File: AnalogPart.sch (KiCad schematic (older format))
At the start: 9 parts, among them U15 LT6018

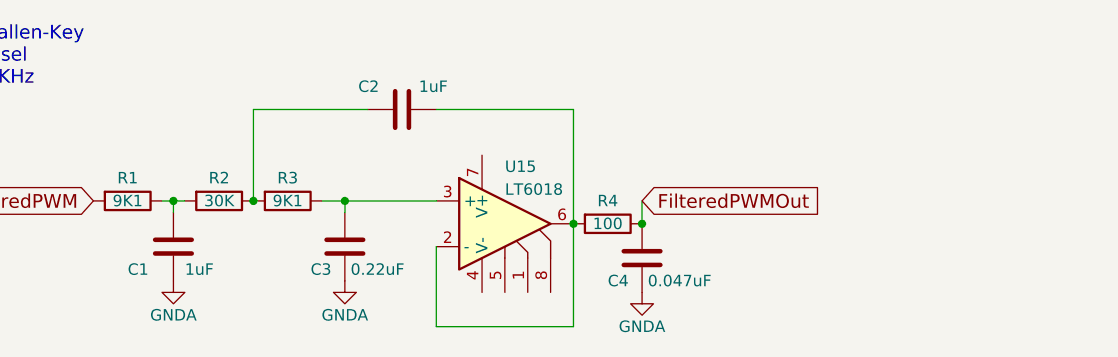
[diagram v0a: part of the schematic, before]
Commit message: Version 1. Directly drive PWM filter using 74hc74 flip flop
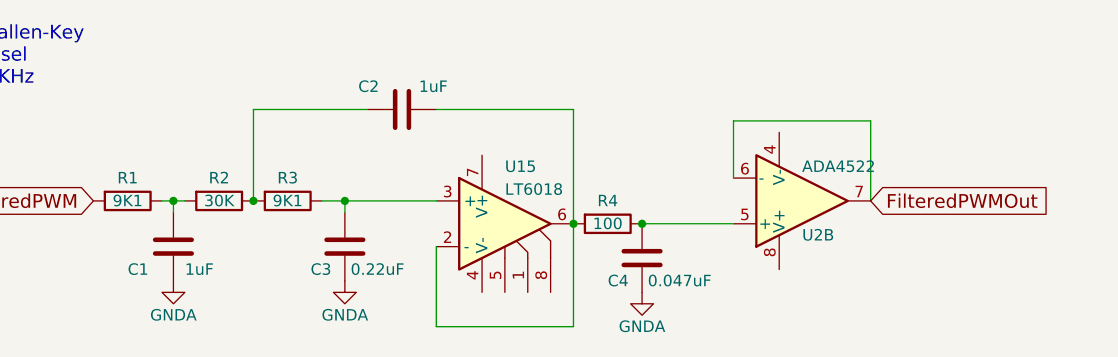
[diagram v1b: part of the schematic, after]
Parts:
- added U2: ADA4522, symbol ADA4075
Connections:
- net FilteredPWMOut: now also U2.6 (-), U2.7; no longer C4.1, R4.1
- new net: C4.1, R4.1, U2.5 (+)
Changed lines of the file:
@@
 $Descr A4 11693 8268
 encoding utf-8
-Sheet 2 3
+Sheet 2 2
 Title ""
 Date ""
@@
 $EndComp
 $Comp
-L GNDA #PWR13
+L GNDA #PWR21
 U 1 1 5A91C21B
 P 2350 2700
-F 0 "#PWR13" H 2350 2450 50  0001 C CNN
+F 0 "#PWR21" H 2350 2450 50  0001 C CNN
 F 1 "GNDA" H 2350 2550 50  0000 C CNN
 F 2 "" H 2350 2700 50  0001 C CNN
@@
 $EndComp
 $Comp
-L GNDA #PWR14
+L GNDA #PWR22
 U 1 1 5A91C23F
 P 3100 2700
-F 0 "#PWR14" H 3100 2450 50  0001 C CNN
+F 0 "#PWR22" H 3100 2450 50  0001 C CNN
 F 1 "GNDA" H 3100 2550 50  0000 C CNN
 F 2 "" H 3100 2700 50  0001 C CNN
@@
 $EndComp
 Wire Wire Line
-	2300 2350 2400 2350
+	2300 2350 2350 2350
+Wire Wire Line
+	2350 2350 2400 2350
 $Comp
 L CA3130 U15
@@
 $EndComp
 Wire Wire Line
-	3000 2350 3500 2350
+	3000 2350 3100 2350
+Wire Wire Line
+	3100 2350 3500 2350
 Wire Wire Line
 	3200 1950 2700 1950
@@
 Text GLabel 2000 2350 0    60   Input ~ 0
 UnfilteredPWM
-Text GLabel 4400 2350 2    60   Input ~ 0
+Text GLabel 5400 2350 2    60   Input ~ 0
 FilteredPWMOut
 Wire Wire Line
@@
 	2350 2400 2350 2350
 Wire Wire Line
-	4100 1950 4100 2900
+	4100 1950 4100 2450
+Wire Wire Line
+	4100 2450 4100 2900
 Wire Wire Line
 	4100 1950 3500 1950
@@
 $EndComp
 $Comp
-L GNDA #PWR15
+L GNDA #PWR23
 U 1 1 5A91EC1A
 P 4400 2750
-F 0 "#PWR15" H 4400 2500 50  0001 C CNN
+F 0 "#PWR23" H 4400 2500 50  0001 C CNN
 F 1 "GNDA" H 4400 2600 50  0000 C CNN
 F 2 "" H 4400 2750 50  0001 C CNN
@@
 	1    0    0    -1
 $EndComp
-Wire Wire Line
-	4400 2350 4400 2450
 Connection ~ 4400 2450
+$Comp
+L ADA4075 U2
+U 2 1 5A94DB7C
+P 5100 2350
+F 0 "U2" H 5100 2500 50  0000 L CNN
+F 1 "ADA4522" H 5100 2200 50  0000 L CNN
+F 2 "" H 5000 2400 50  0001 C CNN
+F 3 "" H 5100 2500 50  0001 C CNN
+	2    5100 2350
+	1    0    0    1
+$EndComp
+Wire Wire Line
+	4800 2000 4800 2250
+Wire Wire Line
+	4800 2000 5400 2000
+Wire Wire Line
+	5400 2000 5400 2350
+Wire Wire Line
+	4400 2450 4800 2450
 $EndSCHEMATC

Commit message: Version 2. Use cmos logic only. Show time budget.
Eschew F85.
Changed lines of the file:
@@
 $EndComp
 $Comp
-L GNDA #PWR21
+L GNDA #PWR23
 U 1 1 5A91C21B
 P 2350 2700
-F 0 "#PWR21" H 2350 2450 50  0001 C CNN
+F 0 "#PWR23" H 2350 2450 50  0001 C CNN
 F 1 "GNDA" H 2350 2550 50  0000 C CNN
 F 2 "" H 2350 2700 50  0001 C CNN
@@
 $EndComp
 $Comp
-L GNDA #PWR22
+L GNDA #PWR24
 U 1 1 5A91C23F
 P 3100 2700
-F 0 "#PWR22" H 3100 2450 50  0001 C CNN
+F 0 "#PWR24" H 3100 2450 50  0001 C CNN
 F 1 "GNDA" H 3100 2550 50  0000 C CNN
 F 2 "" H 3100 2700 50  0001 C CNN
@@
 $EndComp
 Wire Wire Line
-	2300 2350 2350 2350
-Wire Wire Line
-	2350 2350 2400 2350
+	2300 2350 2400 2350
 $Comp
 L CA3130 U15
@@
 $EndComp
 Wire Wire Line
-	3000 2350 3100 2350
-Wire Wire Line
-	3100 2350 3500 2350
+	3000 2350 3500 2350
 Wire Wire Line
 	3200 1950 2700 1950
@@
 	2350 2400 2350 2350
 Wire Wire Line
-	4100 1950 4100 2450
-Wire Wire Line
-	4100 2450 4100 2900
+	4100 1950 4100 2900
 Wire Wire Line
 	4100 1950 3500 1950
@@
 $EndComp
 $Comp
-L GNDA #PWR23
+L GNDA #PWR25
 U 1 1 5A91EC1A
 P 4400 2750
-F 0 "#PWR23" H 4400 2500 50  0001 C CNN
+F 0 "#PWR25" H 4400 2500 50  0001 C CNN
 F 1 "GNDA" H 4400 2600 50  0000 C CNN
 F 2 "" H 4400 2750 50  0001 C CNN

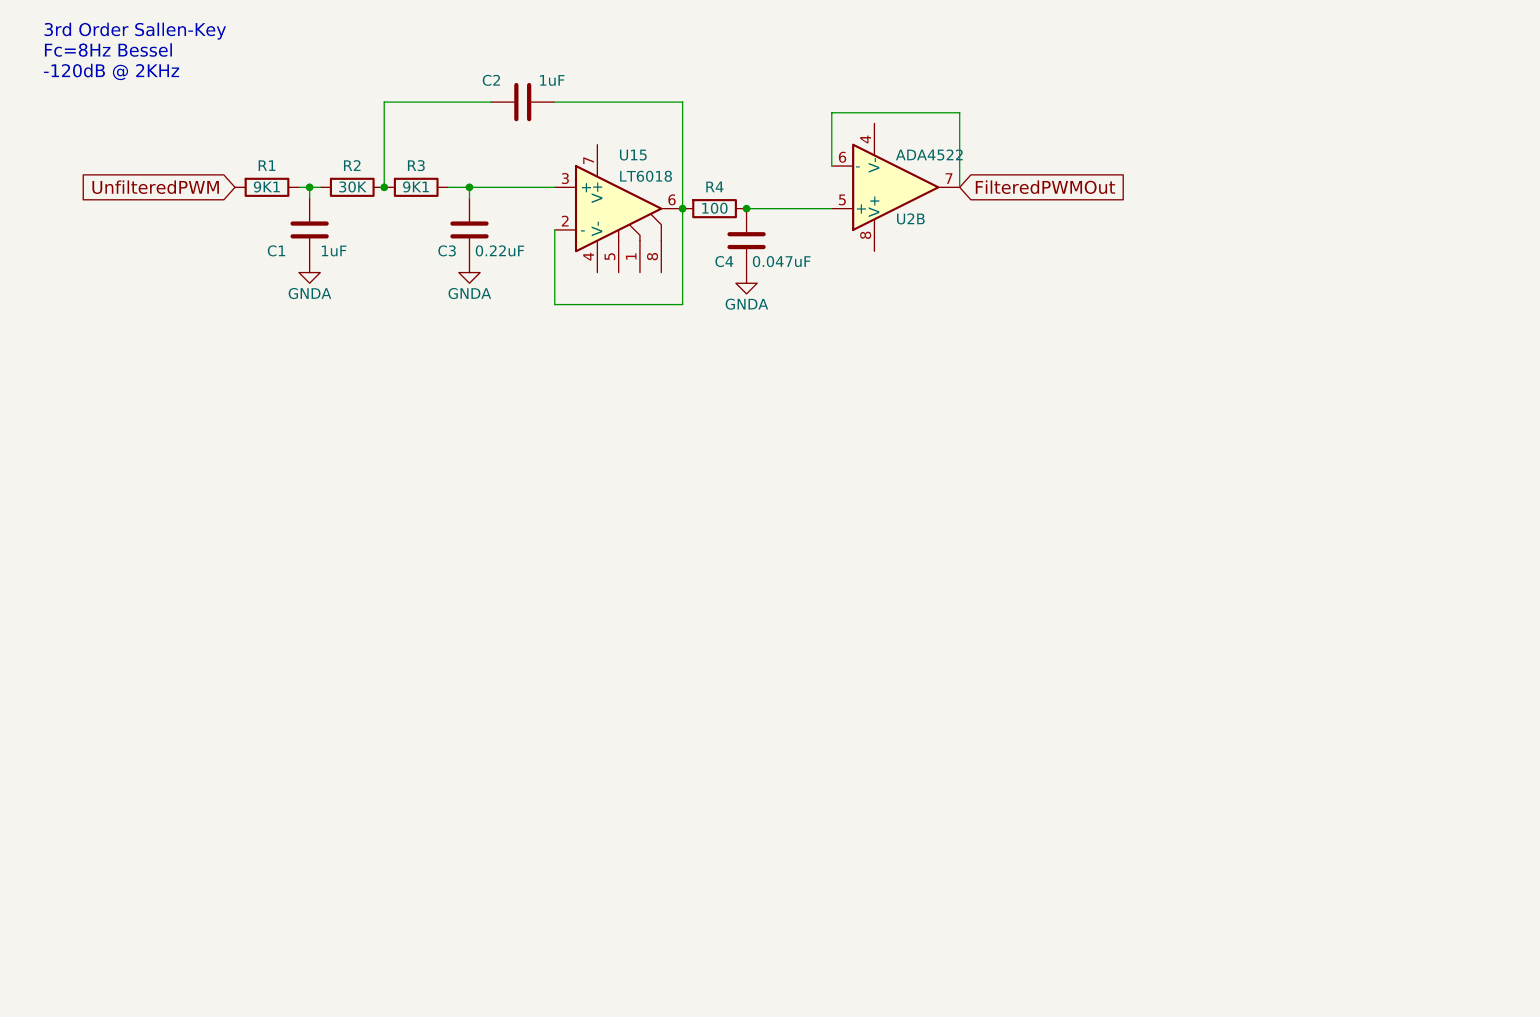
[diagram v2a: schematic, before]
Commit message: Added version 3 files
Tested, working as of 3.25.2018. Tested using IXDD609 gate driver.
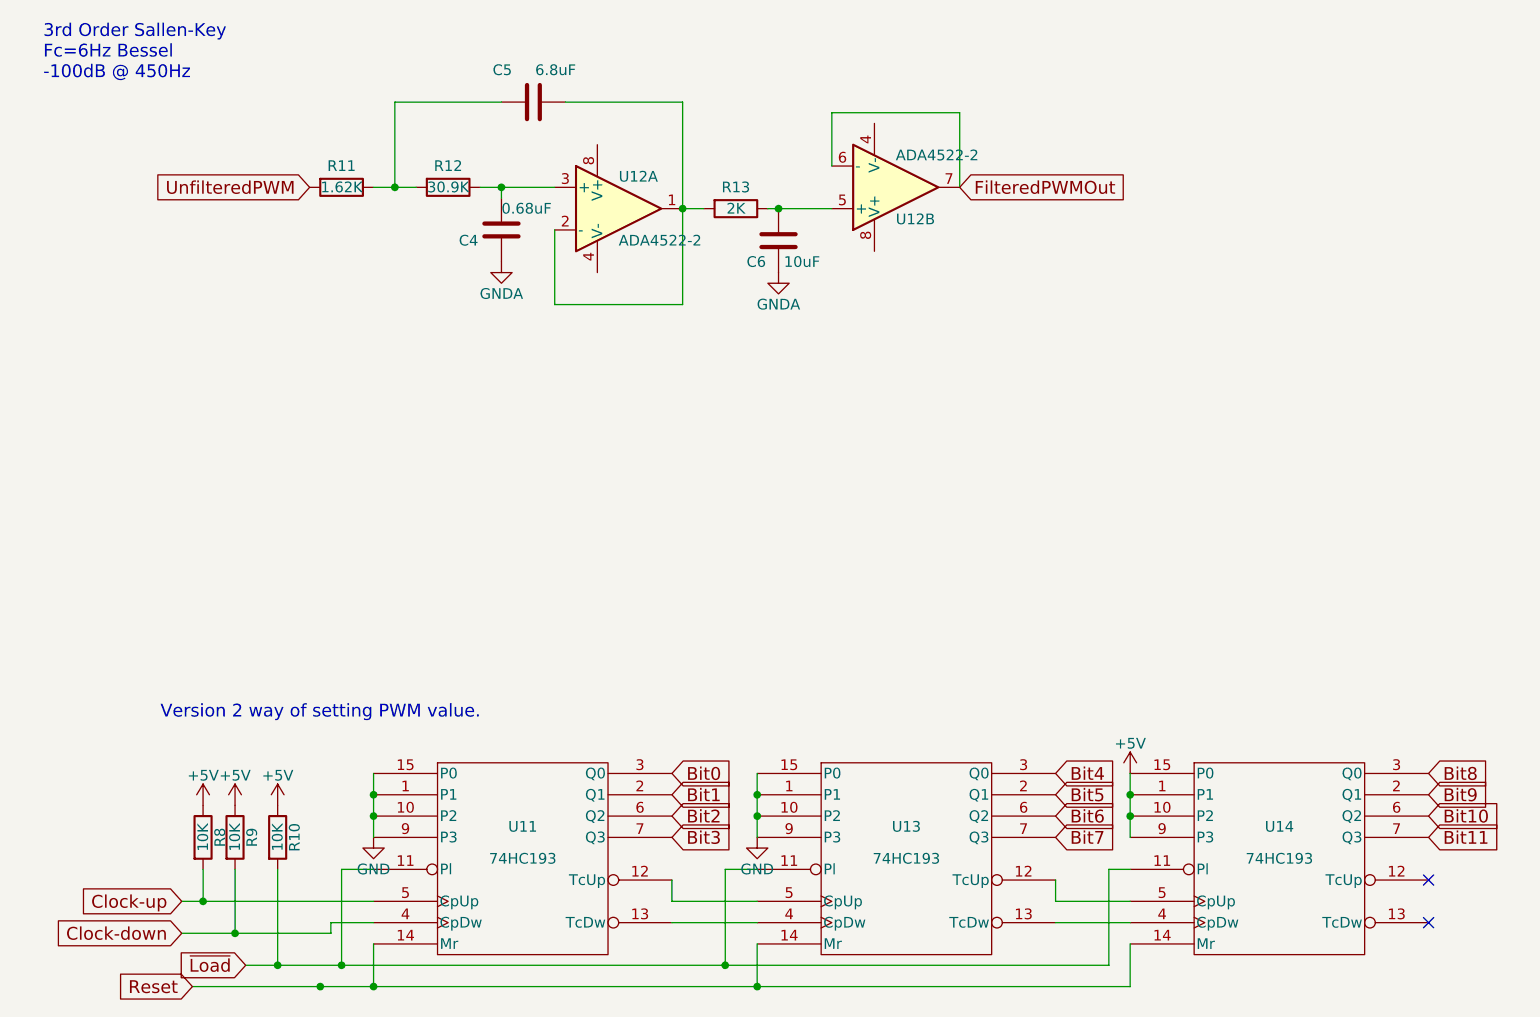
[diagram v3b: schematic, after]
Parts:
- removed C1: 1uF, symbol C
- removed R3: 9K1, symbol R
- removed U15: LT6018, symbol CA3130
- added R10, R8, R9: 10K, symbol R
- added U11, U13, U14: 74HC193, symbol 74LS193
- added unit 1 of U12
- C4: renamed from C3; value 0.22uF -> 0.68uF
- C5: renamed from C2; value 1uF -> 6.8uF
- C6: renamed from C4; value 0.047uF -> 10uF
- R11: renamed from R1; value 9K1 -> 1.62K
- R12: renamed from R2; value 30K -> 30.9K
- R13: renamed from R4; value 100 -> 2K
- U12: renamed from U2; value ADA4522 -> ADA4522-2
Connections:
- net at R11.1, R12.2: now also C5.1
- net at R12.1: now also C4.1, U12.3 (+); no longer C5.1
- net at C5.2, R13.2: now also U12.1, U12.2 (-)
- new net: U11.12 (TcUp), U13.5 (CpUp)
- new net: U11.13 (TcDw), U13.4 (CpDw)
- new net: U13.12 (TcUp), U14.5 (CpUp)
- new net: U13.13 (TcDw), U14.4 (CpDw)
- new net +5V: R10.1, R8.1, R9.1, U14.1 (P1), U14.10 (P2), U14.15 (P0), U14.9 (P3)
- new net Bit0: U11.3 (Q0)
- new net Bit1: U11.2 (Q1)
- new net Bit10: U14.6 (Q2)
- new net Bit11: U14.7 (Q3)
- new net Bit2: U11.6 (Q2)
- new net Bit3: U11.7 (Q3)
- new net Bit4: U13.3 (Q0)
- new net Bit5: U13.2 (Q1)
- new net Bit6: U13.6 (Q2)
- new net Bit7: U13.7 (Q3)
- new net Bit8: U14.3 (Q0)
- new net Bit9: U14.2 (Q1)
- new net Clock-down: R9.2, U11.4 (CpDw)
- new net Clock-up: R8.2, U11.5 (CpUp)
- new net GND: U11.1 (P1), U11.10 (P2), U11.15 (P0), U11.8 (GND), U11.9 (P3), U13.1 (P1), U13.10 (P2), U13.15 (P0), U13.8 (GND), U13.9 (P3), U14.8 (GND)
- new net Reset: U11.14 (Mr), U13.14 (Mr), U14.14 (Mr)
- new net VCC: U11.16 (VCC), U13.16 (VCC), U14.16 (VCC)
- new net ~Load: R10.2, U11.11 (Pl), U13.11 (Pl), U14.11 (Pl)
- no-connect marks 0 -> 2
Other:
- note added: "3rd Order Sallen-Key \nFc=6Hz Bessel\n-100dB @ 450Hz"
- note added: "Version 2 way of setting PWM value."
- note removed: "3rd Order Sallen-Key \nFc=8Hz Bessel\n-120dB @ 2KHz"
- moved on the sheet: C4, C5, C6, R11, R12, R13
